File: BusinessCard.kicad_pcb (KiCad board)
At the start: 2 copper layers, 88.9 x 50.8 mm, 93 parts, among them P1 ButtonPad, P2 ButtonPad, P3 ButtonPad, P4 ButtonPad, Q1 Q_NMOS_DGS

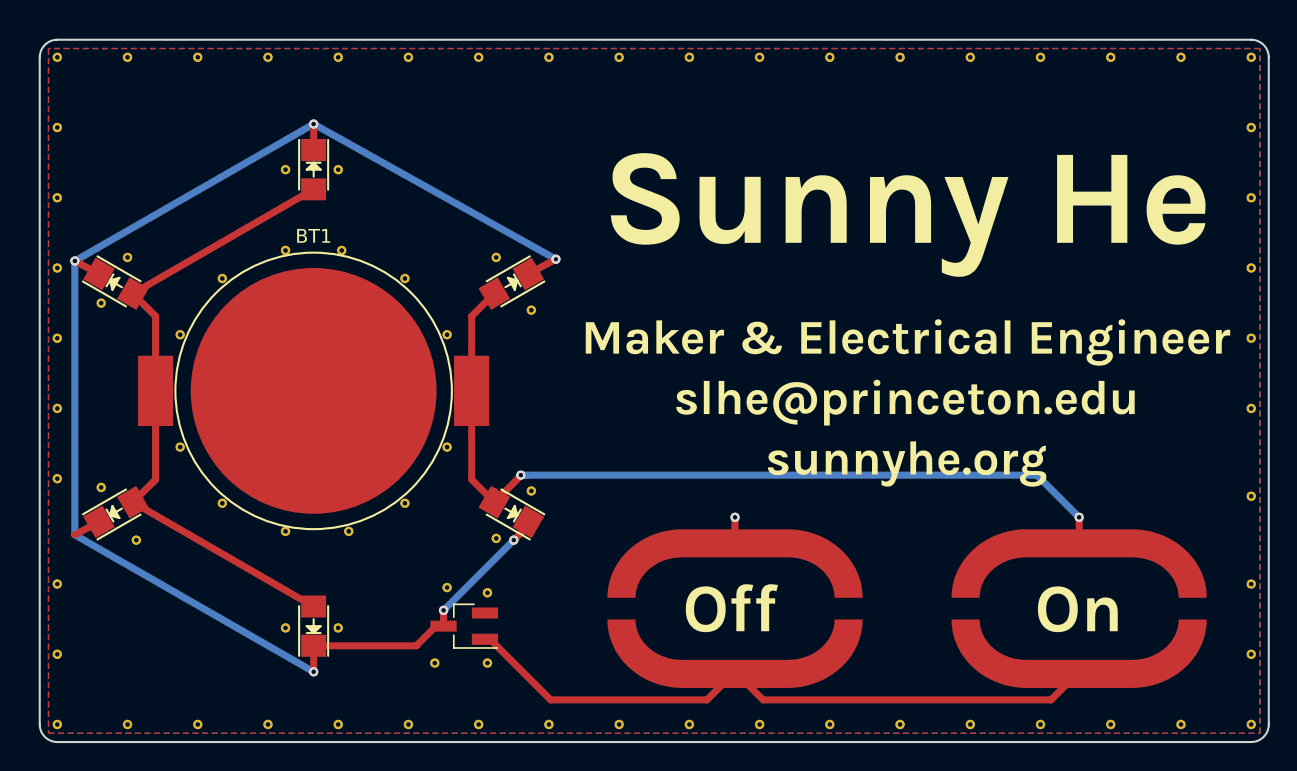
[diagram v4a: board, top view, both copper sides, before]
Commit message: Adjust board size
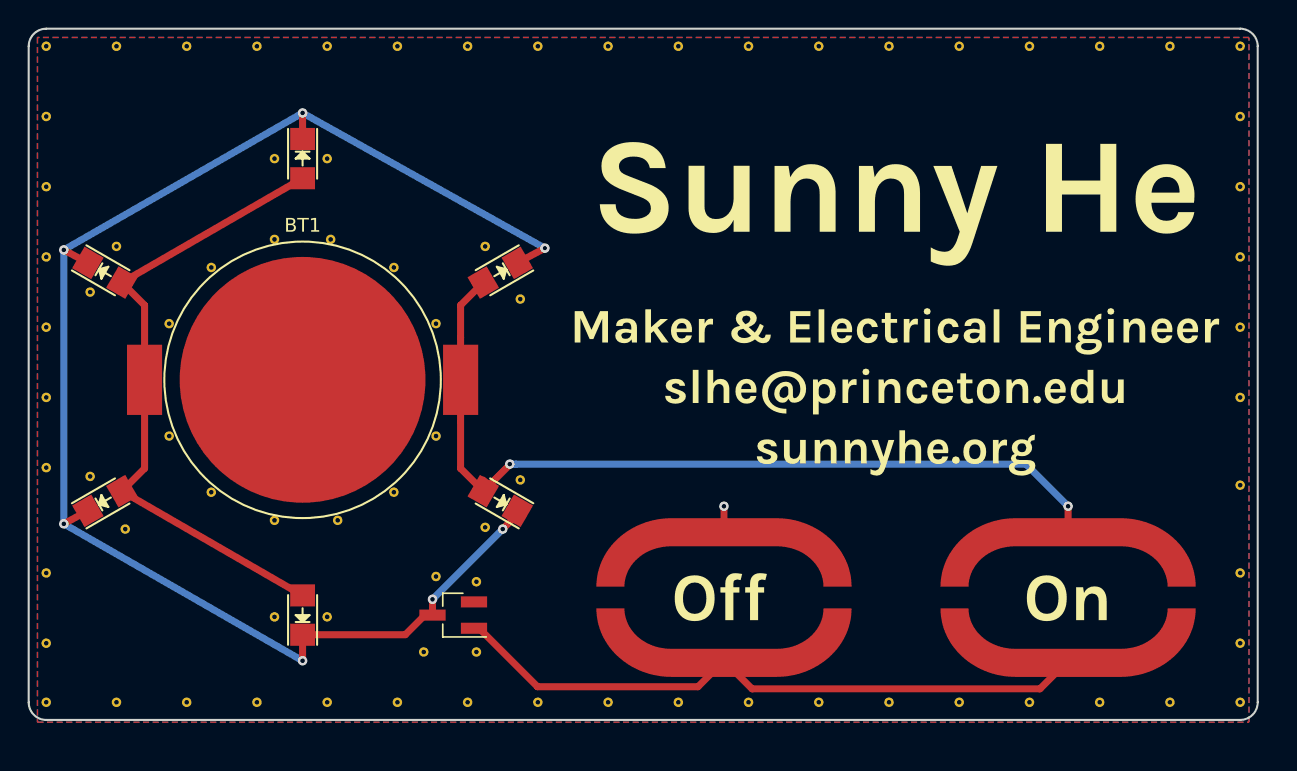
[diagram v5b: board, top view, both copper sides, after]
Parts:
- moved REF** 1.80 mm to (127.5, 98.7)
- moved REF** 1.80 mm to (102.1, 98.7)
- moved REF** 1.80 mm to (97.0, 98.7)
- moved REF** 1.80 mm to (137.6, 98.7)
- moved REF** 1.80 mm to (122.4, 98.7)
- moved REF** 1.80 mm to (117.3, 98.7)
- moved REF** 1.80 mm to (112.2, 98.7)
- moved REF** 1.80 mm to (107.2, 98.7)
- moved REF** 1.80 mm to (91.9, 98.7)
- moved REF** 1.80 mm to (86.8, 98.7)
- moved REF** 1.80 mm to (81.8, 98.7)
- moved REF** 1.80 mm to (76.7, 98.7)
- moved REF** 1.80 mm to (71.6, 98.7)
- moved REF** 1.80 mm to (66.5, 98.7)
- moved REF** 1.80 mm to (61.4, 98.7)
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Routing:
- net Cathode: vias 6 -> 7
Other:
- board size 88.9 x 50.8 mm -> 88.9 x 50 mm

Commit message: Add filtering components, back silkscreen
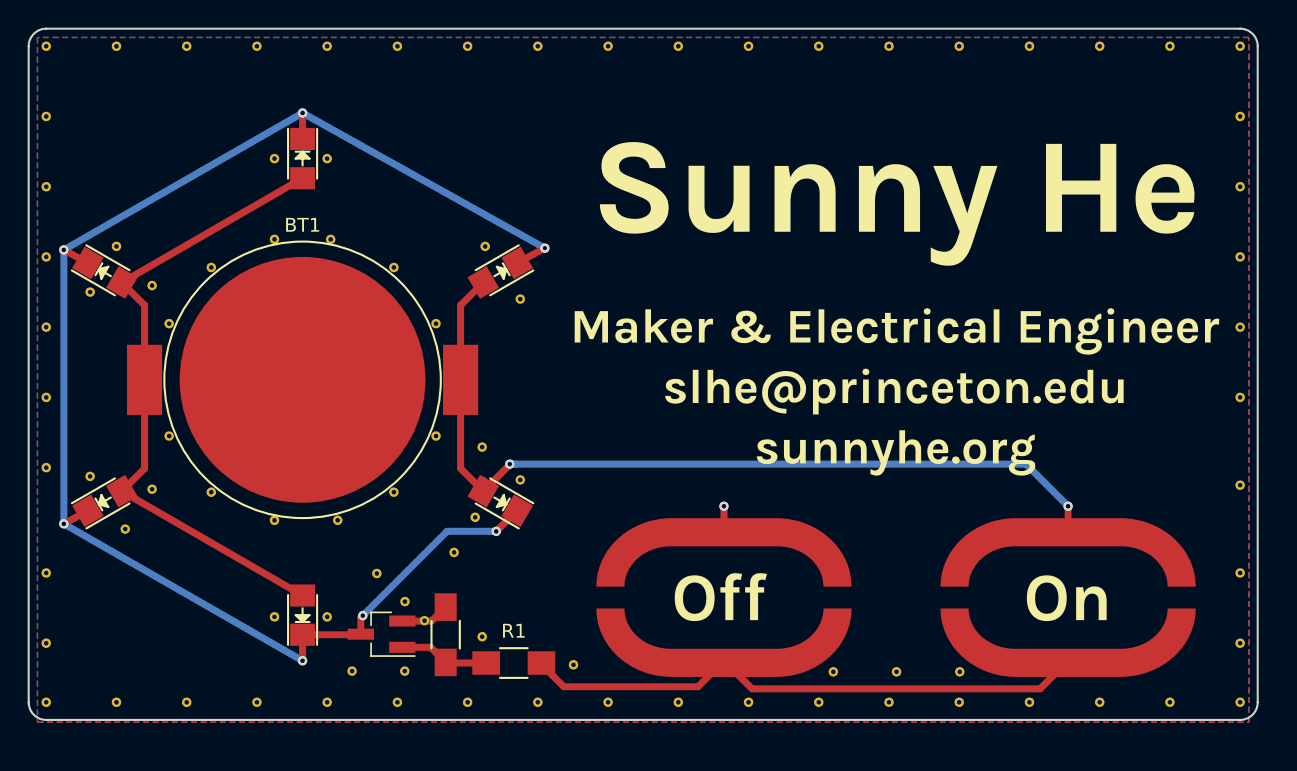
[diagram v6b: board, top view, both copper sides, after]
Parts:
- removed the REF** at (79.5, 89.6)
- removed the REF** at (82.4, 90.0)
- added C1: C, Capacitors_SMD:C_1206_HandSoldering, F.Cu at (80.2, 93.8)
- added G***: LOGO, CardElements:Schematic, B.Cu at (92.5, 75.0)
- added R1: R, Resistors_SMD:R_1206_HandSoldering, F.Cu at (85.1, 95.9)
- added REF**: VIA_13_7, Vias:VIA_13_7, F.Cu at (77.2, 91.4)
- added REF**: VIA_13_7, Vias:VIA_13_7, F.Cu at (75.2, 89.4)
- added REF**: VIA_13_7, Vias:VIA_13_7, F.Cu at (80.8, 87.9)
- added REF**: VIA_13_7, Vias:VIA_13_7, F.Cu at (78.6, 92.8)
- added REF**: VIA_13_7, Vias:VIA_13_7, F.Cu at (58.9, 68.6)
- added REF**: VIA_13_7, Vias:VIA_13_7, F.Cu at (58.9, 83.3)
- added REF**: VIA_13_7, Vias:VIA_13_7, F.Cu at (82.8, 80.3)
- added REF**: VIA_13_7, Vias:VIA_13_7, F.Cu at (112.8, 96.5)
- added REF**: VIA_13_7, Vias:VIA_13_7, F.Cu at (117.3, 96.5)
- added REF**: VIA_13_7, Vias:VIA_13_7, F.Cu at (108.2, 96.5)
- added REF**: VIA_13_7, Vias:VIA_13_7, F.Cu at (82.8, 94.0)
- added REF**: VIA_13_7, Vias:VIA_13_7, F.Cu at (89.4, 96.0)
- moved REF** 5.36 mm to (73.4, 96.5)
- moved REF** 5.36 mm to (77.2, 96.5)
- moved Q1 5.36 mm to (75.5, 93.8)
- moved REF** 1.02 mm to (82.3, 85.3)
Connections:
- Q1 pad 2: Sense -> Net-(C1-Pad1)
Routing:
- net Net-(C1-Pad1): track 0.00 -> 6.90 mm
- net Sense: track 47.2 -> 41.4 mm
- net GND: track 2.03 -> 5.59 mm
- net Cathode: track 110.0 -> 110.8 mm
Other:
- board text added: "OFF"
- board text added: "ON"
